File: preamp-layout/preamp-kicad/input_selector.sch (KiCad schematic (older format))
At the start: 40 parts, among them J51 Conn_01x03_Female, J52 Conn_01x03_Male, J53 Conn_01x03_Male, J54 Conn_01x03_Male, J55 Conn_01x03_Male, J56 Conn_01x03_Male, J57 Conn_01x07_Female, J58 Conn_01x07_Female, J59 Conn_01x03_Male, J60 Conn_01x03_Female, J61 Conn_01x02_Male, J62 Conn_01x02_Male, J63 Conn_01x03_Female, J64 Conn_01x03_Female, K1 G6JU, K2 G6JU, K3 G6JU, K4 G6JU, K5 G6JU, K6 G6JU, K7 G6JU, U10 ULN2003, U11 ULN2003, U9 MCP23S17_SP

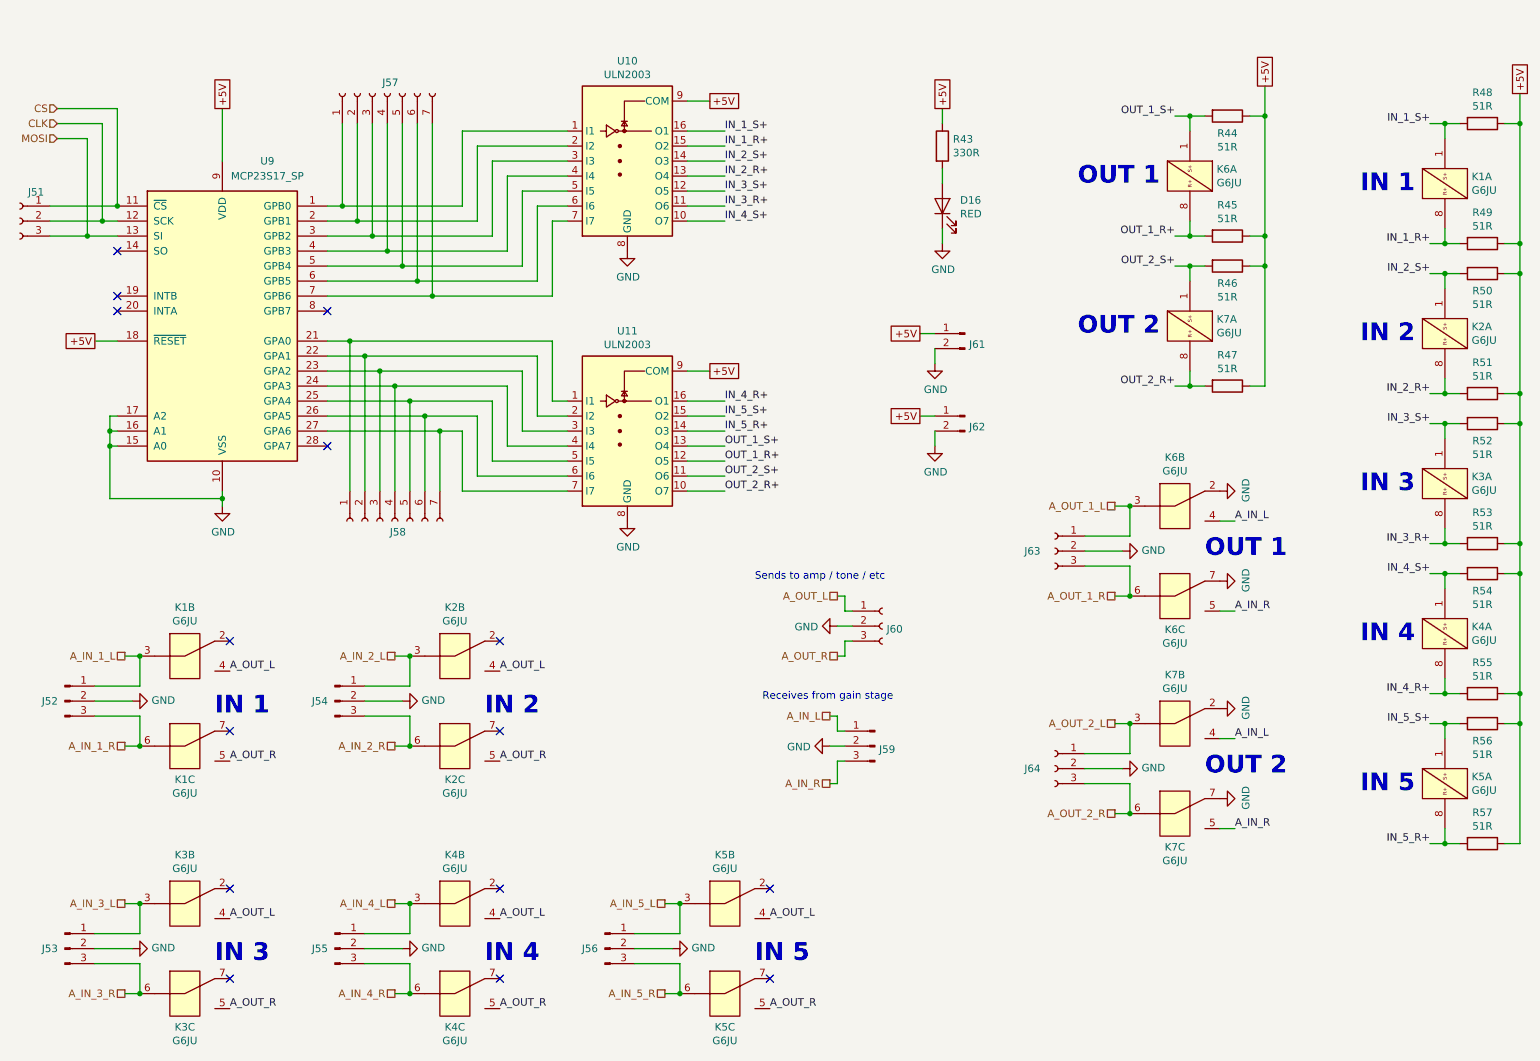
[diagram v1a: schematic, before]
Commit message: BOM Update
parts added to BOM, connector cleanup. Stopping point before renumbering refdes in a more intelligent way.
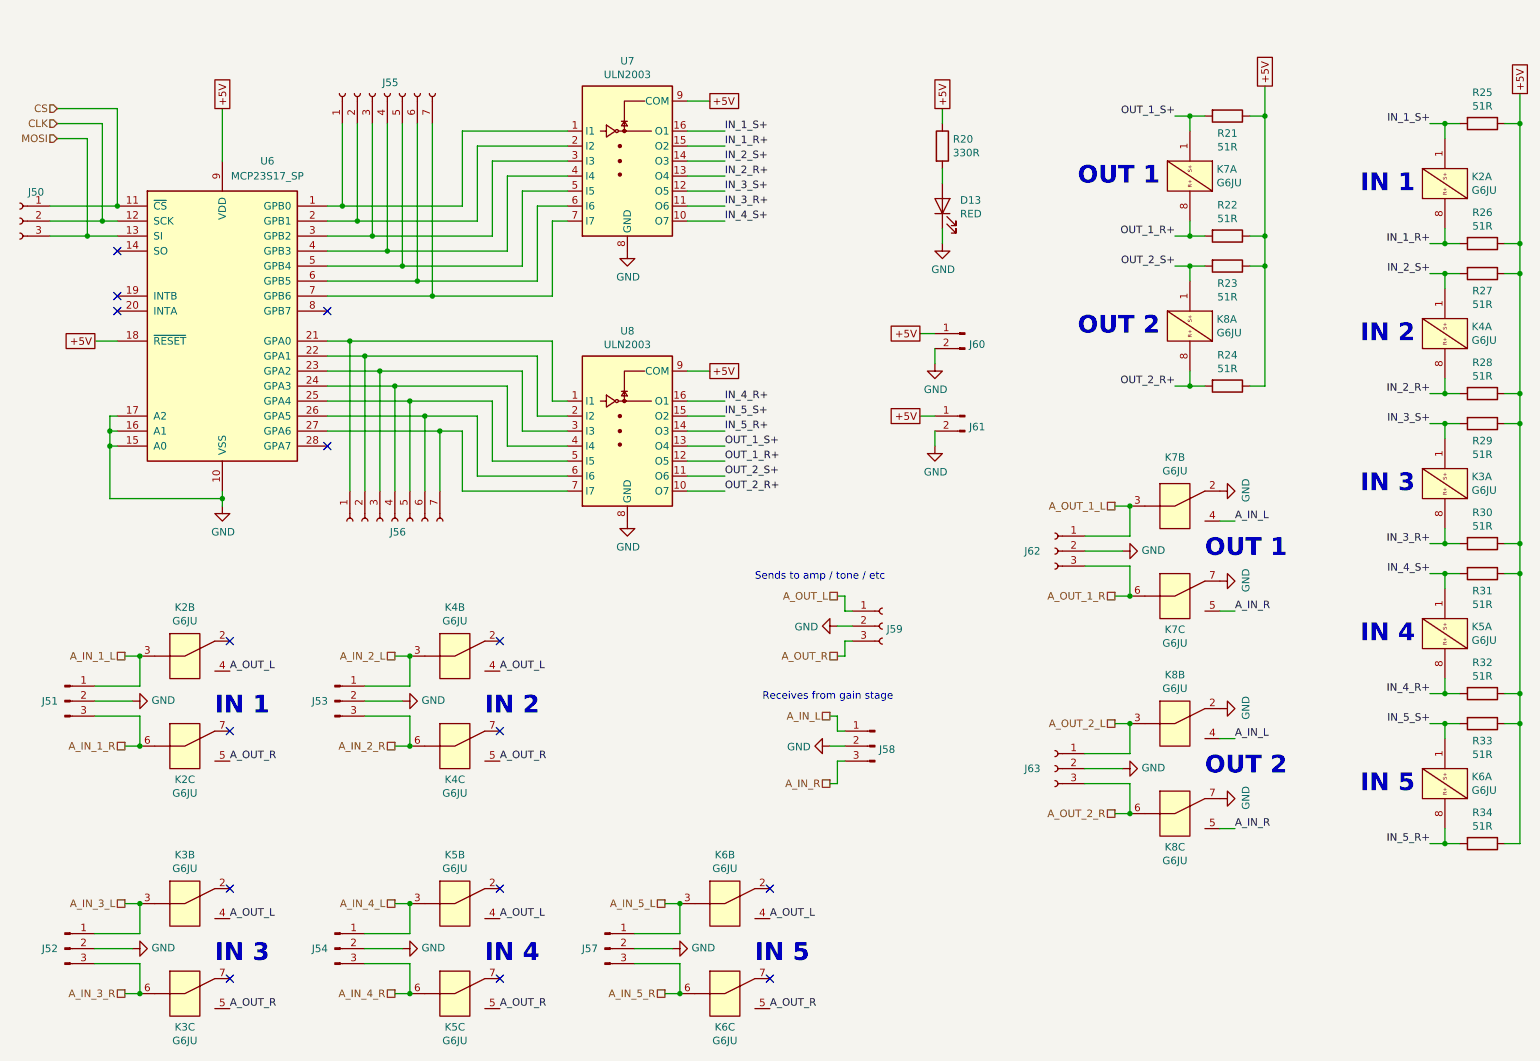
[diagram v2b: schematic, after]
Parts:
- renumbered D16 to D13, J51 to J50, J52 to J51, J53 to J52, J54 to J53, J55 to J54, J57 to J55, J58 to J56, J56 to J57, J59 to J58, J60 to J59, J61 to J60, J62 to J61, J63 to J62, J64 to J63, K1 to K2, K2 to K4, K4 to K5, K5 to K6, K6 to K7, K7 to K8, R43 to R20, R44 to R21, R45 to R22, R46 to R23, R47 to R24, R48 to R25, R49 to R26, R50 to R27, R51 to R28, R52 to R29, R53 to R30, R54 to R31, R55 to R32, R56 to R33, R57 to R34, U9 to U6, U10 to U7, U11 to U8

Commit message: Schematic Redesignation
Regenerated RefDes for all parts, updated BOM accordingly and perfomred check on values, RefDes present from schematic to BOM. Value changes, BOM filled in as a result.
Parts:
- renumbered K4 to K3, K3 to K4
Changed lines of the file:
@@
-	1    0    0    -1
-$EndComp
-$Comp
-L Interface_Expansion:MCP23S17_SP U?
-U 1 1 5E01AA66
-P 2200 2700
-AR Path="/5E01AA66" Ref="U?"  Part="1"
-AR Path="/5E2D8DA2/5E01AA66" Ref="U6"  Part="1"
-F 0 "U6" H 2500 3800 50  0000 C CNN
-F 1 "MCP23S17_SP" H 2500 3700 50  0000 C CNN
-F 2 "Package_DIP:DIP-28_W7.62mm" H 2400 1700 50  0001 L CNN
-F 3 "http://ww1.microchip.com/downloads/en/DeviceDoc/20001952C.pdf" H 2400 1600 50  0001 L CNN
-	1    2200 2700
 	1    0    0    -1
 $EndComp
@@
 Wire Wire Line
 	5450 1200 5300 1200
-Text GLabel 2200 1250 1    50   UnSpc ~ 0
+Text GLabel 2200 1600 1    50   UnSpc ~ 0
 +5V
-Wire Wire Line
-	2200 1250 2200 1600
 Wire Wire Line
 	5300 1400 5550 1400
@@
 Text GLabel 6850 3300 0    50   UnSpc ~ 0
 +5V
-Text HLabel 1100 1350 0    50   Input ~ 0
+Text HLabel 1300 1450 1    50   Input ~ 0
 CLK
-Text HLabel 1100 1250 0    50   Input ~ 0
+Text HLabel 1400 1450 1    50   Input ~ 0
 CS
-Text HLabel 1100 1450 0    50   Input ~ 0
+Text HLabel 1200 1450 1    50   Input ~ 0
 MOSI
 Wire Wire Line
-	1050 2000 1400 2000
-Wire Wire Line
-	1050 1900 1500 1900
-Wire Wire Line
-	1050 2100 1300 2100
-Connection ~ 1300 2100
-Wire Wire Line
-	1300 2100 1500 2100
-Connection ~ 1400 2000
-Wire Wire Line
-	1400 2000 1500 2000
-Connection ~ 1500 1900
-Wire Wire Line
-	1500 1250 1500 1900
-Wire Wire Line
-	1100 1250 1500 1250
-Wire Wire Line
-	1400 1350 1400 2000
-Wire Wire Line
-	1100 1350 1400 1350
-Wire Wire Line
-	1300 1450 1300 2100
-Wire Wire Line
-	1100 1450 1300 1450
+	1050 1900 1400 1900
+Wire Wire Line
+	1050 2100 1200 2100
+Wire Wire Line
+	1200 1450 1200 2100
 Text Label 5550 1900 0    50   ~ 0
 IN_3_R+
@@
 IN 2
 $Comp
-L preamp:G6JU K4
+L preamp:G6JU K3
 U 1 1 6353124F
 P 10350 2750
-F 0 "K4" V 10304 2928 50  0000 L CNN
+F 0 "K3" V 10304 2928 50  0000 L CNN
 F 1 "G6JU" V 10395 2928 50  0000 L CNN
 F 2 "" H 10350 2850 50  0001 C CNN
@@
 IN 3
 $Comp
-L preamp:G6JU K3
+L preamp:G6JU K4
 U 1 1 6365EAC0
 P 10350 3750
-F 0 "K3" V 10304 3928 50  0000 L CNN
+F 0 "K4" V 10304 3928 50  0000 L CNN
 F 1 "G6JU" V 10395 3928 50  0000 L CNN
 F 2 "" H 10350 3850 50  0001 C CNN
@@
 	3450 5100 3450 4900
 $Comp
-L preamp:G6JU K4
+L preamp:G6JU K3
 U 3 1 63D47795
 P 3750 5500
-F 0 "K4" H 3750 5277 50  0000 C CNN
+F 0 "K3" H 3750 5277 50  0000 C CNN
 F 1 "G6JU" H 3750 5186 50  0000 C CNN
 F 2 "" H 3750 5600 50  0001 C CNN
@@
 $EndComp
 $Comp
-L preamp:G6JU K4
+L preamp:G6JU K3
 U 2 1 63D4779F
 P 3750 4900
-F 0 "K4" H 3750 5225 50  0000 C CNN
+F 0 "K3" H 3750 5225 50  0000 C CNN
 F 1 "G6JU" H 3750 5134 50  0000 C CNN
 F 2 "" H 3750 5000 50  0001 C CNN
@@
 	1650 6750 1650 6550
 $Comp
-L preamp:G6JU K3
+L preamp:G6JU K4
 U 3 1 63E1D906
 P 1950 7150
-F 0 "K3" H 1950 6927 50  0000 C CNN
+F 0 "K4" H 1950 6927 50  0000 C CNN
 F 1 "G6JU" H 1950 6836 50  0000 C CNN
 F 2 "" H 1950 7250 50  0001 C CNN
@@
 NoConn ~ 2900 3500
 $Comp
-L preamp:G6JU K3
+L preamp:G6JU K4
 U 2 1 63E1D910
 P 1950 6550
-F 0 "K3" H 1950 6875 50  0000 C CNN
+F 0 "K4" H 1950 6875 50  0000 C CNN
 F 1 "G6JU" H 1950 6784 50  0000 C CNN
 F 2 "" H 1950 6650 50  0001 C CNN
@@
 	1    0    0    -1
 $EndComp
+$Comp
+L Interface_Expansion:MCP23S17_SP U?
+U 1 1 5E01AA66
+P 2200 2700
+AR Path="/5E01AA66" Ref="U?"  Part="1"
+AR Path="/5E2D8DA2/5E01AA66" Ref="U6"  Part="1"
+F 0 "U6" H 2500 3800 50  0000 C CNN
+F 1 "MCP23S17_SP" H 2500 3700 50  0000 C CNN
+F 2 "Package_DIP:DIP-28_W7.62mm" H 2400 1700 50  0001 L CNN
+F 3 "http://ww1.microchip.com/downloads/en/DeviceDoc/20001952C.pdf" H 2400 1600 50  0001 L CNN
+	1    2200 2700
+	1    0    0    -1
+$EndComp
+Wire Wire Line
+	1050 2000 1300 2000
+Wire Wire Line
+	1300 1450 1300 2000
+Wire Wire Line
+	1400 1450 1400 1900
+Connection ~ 1200 2100
+Connection ~ 1300 2000
+Connection ~ 1400 1900
+Wire Wire Line
+	1400 1900 1500 1900
+Wire Wire Line
+	1200 2100 1500 2100
+Wire Wire Line
+	1300 2000 1500 2000
 $EndSCHEMATC

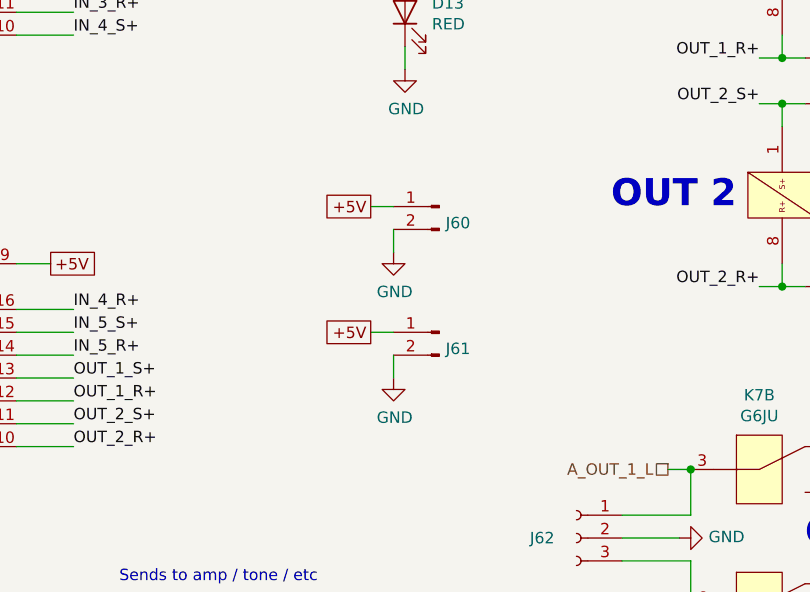
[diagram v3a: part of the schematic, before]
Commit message: Headphone Amp Update
Removed IC buffer on headphone amp schematic. Reconfigured connectors to crossfeed board so that input/output can be easily jumpered.
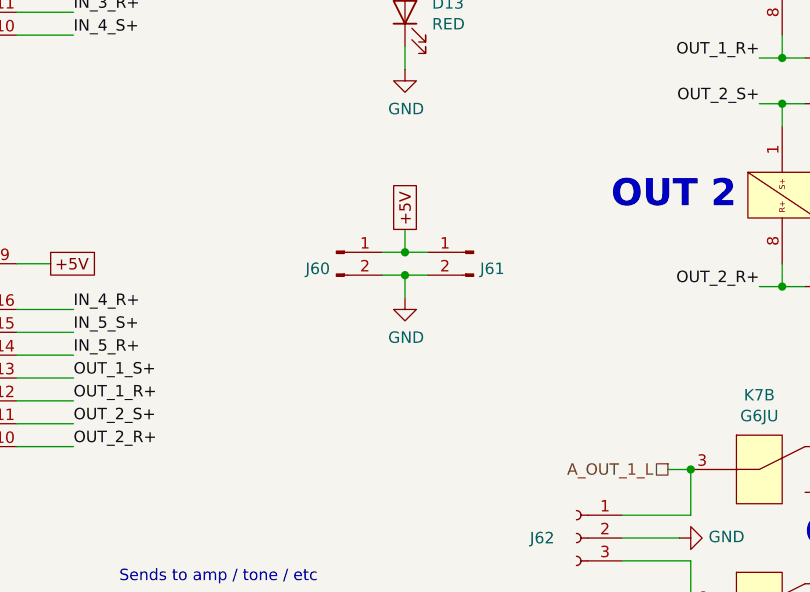
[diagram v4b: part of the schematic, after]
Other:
- moved on the sheet: J60, J61
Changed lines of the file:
@@
 Wire Wire Line
 	7000 2050 7000 2150
-Wire Wire Line
-	6950 3400 6950 3500
-Wire Wire Line
-	6850 3300 6950 3300
-Text GLabel 6850 3300 0    50   UnSpc ~ 0
-+5V
 Text HLabel 1300 1450 1    50   Input ~ 0
 CLK
@@
 Text Notes 5800 5200 0    50   ~ 0
 Receives from gain stage
-Wire Wire Line
-	6950 2850 6950 2950
-Wire Wire Line
-	6850 2750 6950 2750
-Text GLabel 6850 2750 0    50   UnSpc ~ 0
-+5V
 Text Label 5550 3800 0    50   ~ 0
 OUT_2_R+
@@
 L Connector:Conn_01x02_Male J61
 U 1 1 60B85B38
-P 7150 3300
-F 0 "J61" H 7122 3228 50  0000 R CNN
-F 1 "Conn_01x02_Male" H 7122 3183 50  0001 R CNN
-F 2 "Connector_JST:JST_EH_B2B-EH-A_1x02_P2.50mm_Vertical" H 7150 3300 50  0001 C CNN
-F 3 "~" H 7150 3300 50  0001 C CNN
-	1    7150 3300
+P 7300 2950
+F 0 "J61" H 7272 2878 50  0000 R CNN
+F 1 "Conn_01x02_Male" H 7272 2833 50  0001 R CNN
+F 2 "Connector_JST:JST_EH_B2B-EH-A_1x02_P2.50mm_Vertical" H 7300 2950 50  0001 C CNN
+F 3 "~" H 7300 2950 50  0001 C CNN
+	1    7300 2950
 	-1   0    0    -1
 $EndComp
@@
 F 3 "" H 7000 2150 50  0001 C CNN
 	1    7000 2150
-	1    0    0    -1
-$EndComp
-$Comp
-L power:GND #PWR?
-U 1 1 64C83DF6
-P 6950 2950
-AR Path="/5E26F6FE/64C83DF6" Ref="#PWR?"  Part="1"
-AR Path="/5E2D8DA2/64C83DF6" Ref="#PWR059"  Part="1"
-F 0 "#PWR059" H 6950 2700 50  0001 C CNN
-F 1 "GND" H 6955 2777 50  0000 C CNN
-F 2 "" H 6950 2950 50  0001 C CNN
-F 3 "" H 6950 2950 50  0001 C CNN
-	1    6950 2950
-	1    0    0    -1
-$EndComp
-$Comp
-L power:GND #PWR?
-U 1 1 64CA86A4
-P 6950 3500
-AR Path="/5E26F6FE/64CA86A4" Ref="#PWR?"  Part="1"
-AR Path="/5E2D8DA2/64CA86A4" Ref="#PWR060"  Part="1"
-F 0 "#PWR060" H 6950 3250 50  0001 C CNN
-F 1 "GND" H 6955 3327 50  0000 C CNN
-F 2 "" H 6950 3500 50  0001 C CNN
-F 3 "" H 6950 3500 50  0001 C CNN
-	1    6950 3500
 	1    0    0    -1
 $EndComp
@@
 L Connector:Conn_01x02_Male J60
 U 1 1 5E5DB820
-P 7150 2750
-F 0 "J60" H 7122 2678 50  0000 R CNN
-F 1 "Conn_01x02_Male" H 7122 2633 50  0001 R CNN
-F 2 "Connector_JST:JST_EH_B2B-EH-A_1x02_P2.50mm_Vertical" H 7150 2750 50  0001 C CNN
-F 3 "~" H 7150 2750 50  0001 C CNN
-	1    7150 2750
-	-1   0    0    -1
+P 6700 2950
+F 0 "J60" H 6672 2878 50  0000 R CNN
+F 1 "Conn_01x02_Male" H 6672 2833 50  0001 R CNN
+F 2 "Connector_JST:JST_EH_B2B-EH-A_1x02_P2.50mm_Vertical" H 6700 2950 50  0001 C CNN
+F 3 "~" H 6700 2950 50  0001 C CNN
+	1    6700 2950
+	1    0    0    -1
 $EndComp
 $Comp
@@
 Wire Wire Line
 	1300 2000 1500 2000
+Text GLabel 7000 2850 1    50   UnSpc ~ 0
++5V
+Wire Wire Line
+	7100 3050 7000 3050
+Wire Wire Line
+	7000 3050 7000 3150
+Wire Wire Line
+	7100 2950 7000 2950
+$Comp
+L power:GND #PWR?
+U 1 1 60248FFE
+P 7000 3150
+AR Path="/6009D432/60248FFE" Ref="#PWR?"  Part="1"
+AR Path="/5E2D8DA2/60248FFE" Ref="#PWR?"  Part="1"
+F 0 "#PWR?" H 7000 2900 50  0001 C CNN
+F 1 "GND" H 7005 2977 50  0000 C CNN
+F 2 "" H 7000 3150 50  0001 C CNN
+F 3 "" H 7000 3150 50  0001 C CNN
+	1    7000 3150
+	1    0    0    -1
+$EndComp
+Connection ~ 7000 3050
+Wire Wire Line
+	7000 3050 6900 3050
+Wire Wire Line
+	7000 2850 7000 2950
+Connection ~ 7000 2950
+Wire Wire Line
+	7000 2950 6900 2950
 $EndSCHEMATC
